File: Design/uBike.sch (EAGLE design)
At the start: 100 parts, among them J10 455-1750-1-ND, J5 C167321, J6 C111196, J9 CONN_08, Q1 B772, Q2 B772, U1 RA-02_LORA, U10 MAX17048, U2 RP2040, U3 W25QXX128MBIT, U4 TMP102, U5 PAM2401, U6 AMS1117-3.3, U8 MCP73831, U9 LSM6DS0, Y1 12MHz

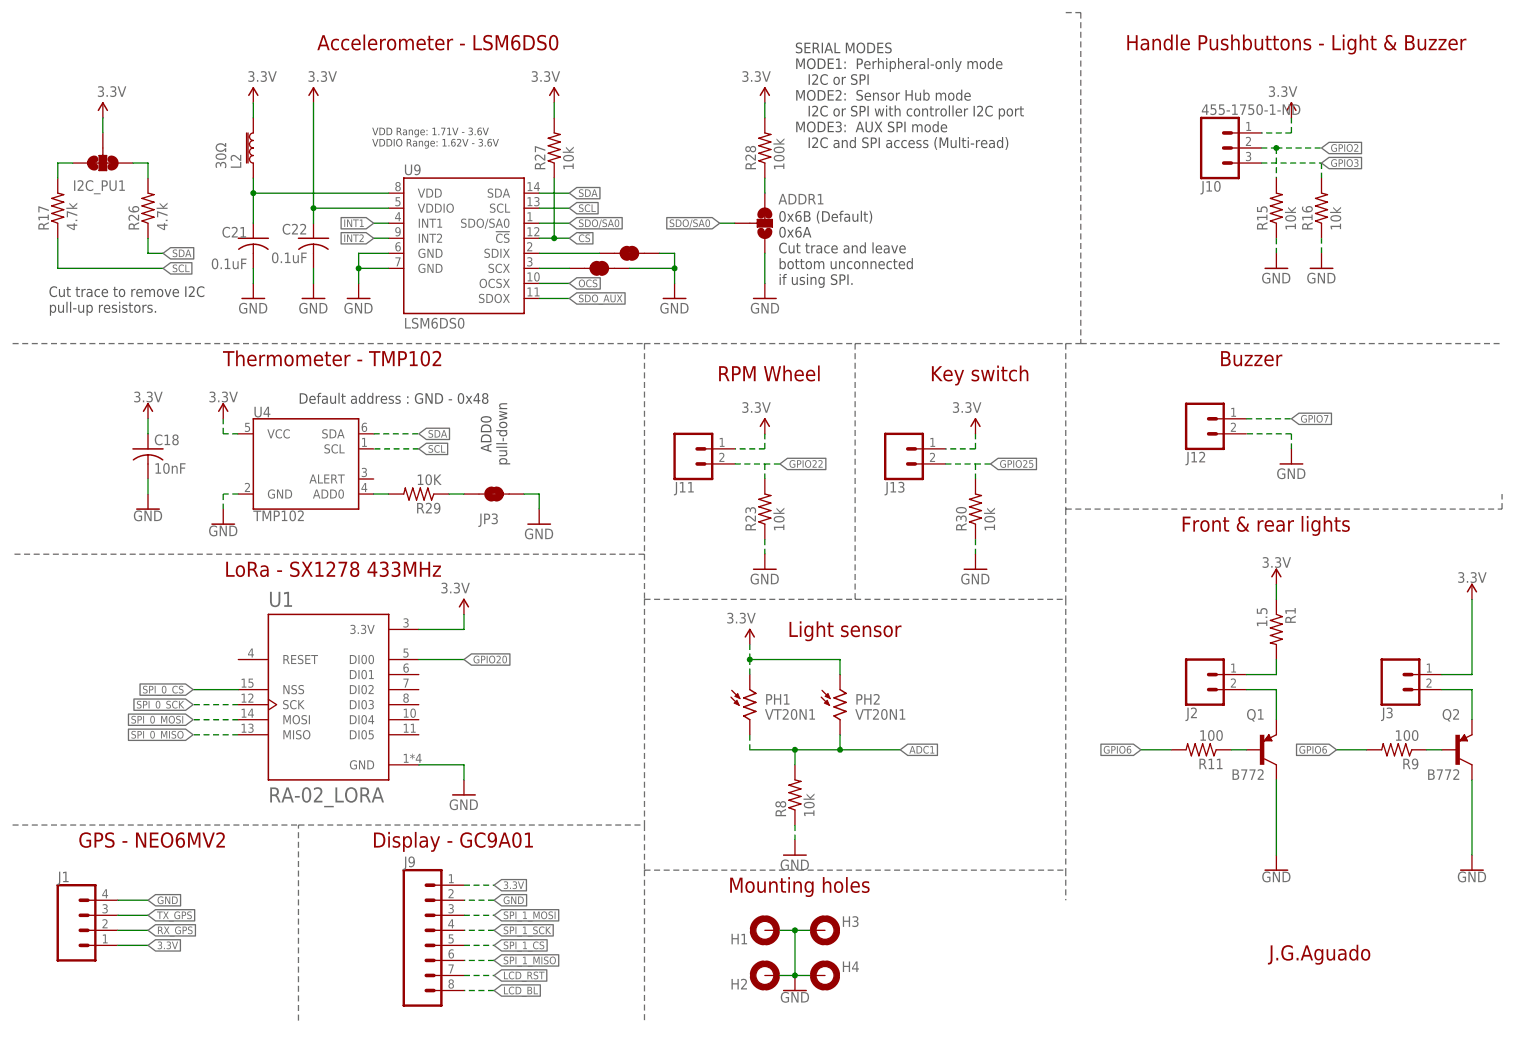
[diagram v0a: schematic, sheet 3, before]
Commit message: New branch replacing Accel & Temp IC with pre-assembled module.
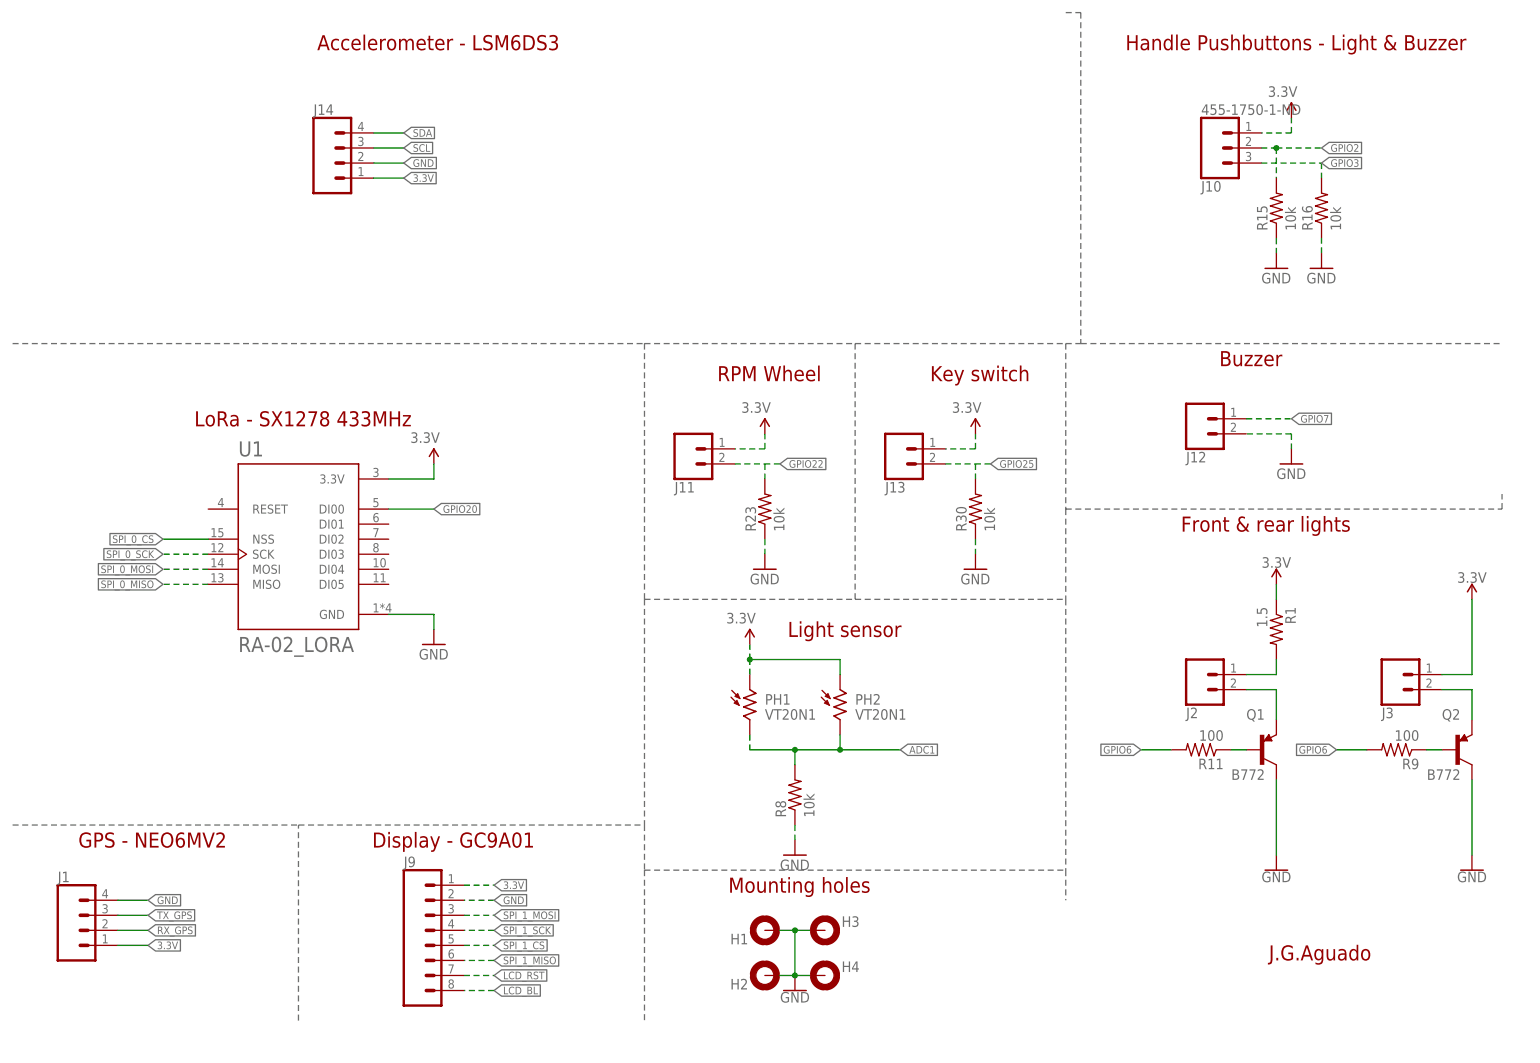
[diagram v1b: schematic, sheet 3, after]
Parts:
- removed ADDR1: JUMPER-SMT_3_1-NC_TRACE_SILK, SparkFun-Jumpers:JUMPER-SMT_3_1-NC_TRACE_SILK
- removed C18: 10nF, rcl:C-USC0402
- removed C21, C22: 0.1uF, rcl:C-USC0402
- removed I2C_PU1: S_MODE, SparkFun-Jumpers:JUMPER-SMT_3_2-NC_TRACE_SILK
- removed JP3: ADD0, SparkFun-Passives:JUMPER-PAD-2-NC_BY_TRACE
- removed L2: 30Ω, SparkFun-Coils:FERRITE_BEAD-0603-30OHM-100MHZ
- removed R17, R26: 4.7k, rcl:R-US_R0402
- removed R27: 10k, rcl:R-US_R0402
- removed R28: 100k, rcl:R-US_R0402
- removed R29: 10K, rcl:R-US_R0402
- removed SDX, SDX1: JUMPER-SMT_2_NC_TRACE_SILK, SparkFun-Jumpers:JUMPER-SMT_2_NC_TRACE_SILK
- removed U4: TMP102, SparkFun-Sensors:TMP102
- removed U9: LSM6DS0, temp:LSM6DS0
- added J14: (no value), SparkFun-Connectors:CONN_04PTH
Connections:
- removed net !CS!: R27.1, U9.!CS!
- removed net ADD0: R29.2, U4.ADD0
- removed net INT1: U9.INT1
- removed net INT2: U9.INT2
- removed net N$15: JP3.1, R29.1
- removed net N$19: I2C_PU1.1, R17.2
- removed net N$20: I2C_PU1.3, R26.2
- removed net N$21: ADDR1.3, R28.1
- removed net OCS: U9.OCSX
- removed net SCX: SDX.2, U9.SCX
- removed net SDI_AUX: SDX1.2, U9.SDIX
- removed net SDO/SA0: ADDR1.2, U9.SDO/SA0
- removed net SDO_AUX: U9.SDOX
- removed net VDD1: C21.1, L2.2, U9.VDD
- net 3.3V: now also J14.1; no longer C18.1, C22.1, I2C_PU1.2, L2.1, R27.2, R28.2, U4.VCC, U9.VDDIO
- net GND: now also J14.2; no longer ADDR1.1, C18.2, C21.2, C22.2, JP3.2, SDX.1, SDX1.1, U4.GND, U9.GND@6, U9.GND@7
- net SCL: now also J14.3; no longer R17.1, U4.SCL, U9.SCL
- net SDA: now also J14.4; no longer R26.1, U4.SDA, U9.SDA
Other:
- note added: "Accelerometer - LSM6DS3"
- note removed: "0x6B (Default) 0x6A Cut trace and leave bottom unconnected if using SPI."
- note removed: "ADD0 pull-down"
- note removed: "Accelerometer - LSM6DS0"
- note removed: "Cut trace to remove I2C pull-up resistors."
- note removed: "Default address : GND - 0x48"
- note removed: "SERIAL MODES MODE1: Perhipheral-only mode I2C or SPI MODE2: Sensor Hub mode I2C or SPI with controller I2C port MODE3: AUX SPI mode I2C and SPI access (Multi-read)"
- note removed: "Thermometer - TMP102"
- note removed: "VDD Range: 1.71V - 3.6V VDDIO Range: 1.62V - 3.6V"
- moved on the sheet: U1

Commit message: Fixed U3 component with W25Q128JVSIQ
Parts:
- C1, C2: LCSC (none) -> C1548
- C10, C17, C20, C3, C4, C5, C6, C7, C8, C9: value 0.1uF -> 100nF
- C12, C16, C19, C29: LCSC (none) -> C12530
- C23, C24: LCSC (none) -> C7171
- D6: LCSC (none) -> C72038
- D7, D8: LCSC (none) -> C64982
- H1, H2, H3, H4: value MOUNT-PAD-ROUND3.0 -> MOUNT-PAD-ROUND; device holes:MOUNT-PAD-ROUND3.0 -> SpaceDIY_connectors:MOUNT-PAD-ROUND
- J5: LCSC (none) -> C167321
- L3, U2: LCSC (none) -> C135262
- Q1, Q2: LCSC (none) -> C24278
- R1: value 1.5 -> 1; LCSC (none) -> C17928
- R25: value 2.0k -> 2k
- S1, S2: LCSC (none) -> C318884
- U3: value W25QXX128MBIT -> W25Q128JVSIQ; device SparkFun-IC-Memory:W25QXX128MBIT-6X5-SKINNY_CENTER -> SamacSys_Parts:W25Q128JVSIQ
- U5: LCSC (none) -> C508238
- Y1: LCSC (none) -> C9002
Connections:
- net 3.3V: now also U3.VCC; no longer U3.VDD
- net QSPI-0: now also U3.DI_(IO0); no longer U3.D0/DI
- net QSPI-1: now also U3.DO_(IO1); no longer U3.D1/DO
- net QSPI-2: now also U3./WP_(IO2); no longer U3.D2/!WP!
- net QSPI-3: now also U3./HOLD_OR_/RESET_(IO3); no longer U3.D3/!HOLD!
- net QSPI-CS: now also U3./CS; no longer U3.!CS!
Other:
- moved on the sheet: C16, C5, J11, J12, J13, J14, J2, J3, PH1, PH2, Q1, Q2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

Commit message: Updated schematic
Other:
- note removed: "J.G.Aguado"
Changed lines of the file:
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@@
 </classes>
 <parts>
-<part name="FRAME1" library="frames" library_urn="urn:adsk.eagle:library:229" deviceset="A4L-LOC" device=""/>
 <part name="H1" library="SpaceDIY_connectors" deviceset="MOUNT-PAD-ROUND" device="" package3d_urn="urn:adsk.eagle:package:14280/1"/>
 <part name="H2" library="SpaceDIY_connectors" deviceset="MOUNT-PAD-ROUND" device="" package3d_urn="urn:adsk.eagle:package:14280/1"/>
@@
 <part name="R11" library="rcl" library_urn="urn:adsk.eagle:library:334" deviceset="R-US_" device="R0402" package3d_urn="urn:adsk.eagle:package:23547/3" value="100"/>
 <part name="GND4" library="SparkFun-PowerSymbols" deviceset="GND" device=""/>
-<part name="FRAME2" library="frames" library_urn="urn:adsk.eagle:library:229" deviceset="A4L-LOC" device=""/>
 <part name="R20" library="rcl" library_urn="urn:adsk.eagle:library:334" deviceset="R-US_" device="R0603" package3d_urn="urn:adsk.eagle:package:23555/3" value="750K"/>
 <part name="R21" library="rcl" library_urn="urn:adsk.eagle:library:334" deviceset="R-US_" device="R0402" package3d_urn="urn:adsk.eagle:package:23547/3" value="100k"/>
@@
 <part name="U1" library="SpaceDIY_modules" deviceset="RA-02_LORA" device=""/>
 <part name="J1" library="SparkFun-Connectors" deviceset="CONN_04" device="PTH"/>
-<part name="FRAME3" library="frames" library_urn="urn:adsk.eagle:library:229" deviceset="A4L-LOC" device=""/>
 <part name="D6" library="SparkFun-LED" deviceset="LED-YELLOW" device="0603" value="Yellow">
 <attribute name="LCSC" value="C72038"/>
@@
 <part name="GND26" library="SparkFun-PowerSymbols" deviceset="GND" device=""/>
 <part name="SUPPLY33" library="SparkFun-PowerSymbols" deviceset="3.3V" device=""/>
+<part name="FRAME1" library="SpaceDIY_symbols" deviceset="A4L-LOC" device=""/>
+<part name="FRAME2" library="SpaceDIY_symbols" deviceset="A4L-LOC" device=""/>
+<part name="FRAME3" library="SpaceDIY_symbols" deviceset="A4L-LOC" device=""/>
 </parts>
 <sheets>
 <sheet>
 <plain>
-<text x="217.17" y="15.24" size="2.54" layer="94">J.G.Aguado</text>
 <wire x1="160.02" y1="175.26" x2="160.02" y2="129.54" width="0.254" layer="95" style="longdash"/>
 <text x="146.304" y="115.316" size="1.27" layer="97" align="center">PIO must be contiguous
@@
 </plain>
 <instances>
-<instance part="FRAME1" gate="G$1" x="0" y="0" smashed="yes">
-<attribute name="DRAWING_NAME" x="217.17" y="20.32" size="2.54" layer="94"/>
-<attribute name="LAST_DATE_TIME" x="217.17" y="10.16" size="2.286" layer="94"/>
-<attribute name="SHEET" x="248.285" y="5.08" size="2.54" layer="94"/>
-</instance>
 <instance part="C1" gate="G$1" x="48.26" y="101.6" smashed="yes" rot="R90">
 <attribute name="NAME" x="41.656" y="101.854" size="1.778" layer="95" font="vector"/>
@@
 <instance part="SUPPLY33" gate="G$1" x="243.84" y="99.06" smashed="yes">
 <attribute name="VALUE" x="243.84" y="101.854" size="1.778" layer="96" align="bottom-center"/>
+</instance>
+<instance part="FRAME1" gate="G$1" x="0" y="0" smashed="yes">
+<attribute name="LAST_DATE_TIME" x="217.17" y="10.16" size="2.286" layer="94"/>
+<attribute name="SHEET" x="227.965" y="5.08" size="2.54" layer="94"/>
+<attribute name="DRAWING_NAME" x="217.17" y="20.32" size="2.54" layer="94"/>
 </instance>
 </instances>
@@
 <wire x1="129.54" y1="81.28" x2="129.54" y2="91.44" width="0.1524" layer="95" style="longdash"/>
 <wire x1="162.56" y1="25.4" x2="162.56" y2="91.44" width="0.1524" layer="95" style="longdash"/>
-<text x="217.17" y="15.24" size="2.54" layer="94">J.G.Aguado</text>
 </plain>
 <instances>
-<instance part="FRAME3" gate="G$1" x="0" y="0" smashed="yes">
-<attribute name="DRAWING_NAME" x="217.17" y="20.32" size="2.54" layer="94"/>
-<attribute name="LAST_DATE_TIME" x="217.17" y="10.16" size="2.286" layer="94"/>
-<attribute name="SHEET" x="248.285" y="5.08" size="2.54" layer="94"/>
-</instance>
 <instance part="R20" gate="G$1" x="76.2" y="50.8" smashed="yes" rot="R90">
 <attribute name="NAME" x="74.7014" y="46.99" size="1.778" layer="95" rot="R90"/>
@@
 <attribute name="NAME" x="203.2" y="58.42" size="1.778" layer="95"/>
 <attribute name="VALUE" x="203.2" y="55.88" size="1.778" layer="96"/>
+</instance>
+<instance part="FRAME2" gate="G$1" x="0" y="0" smashed="yes">
+<attribute name="LAST_DATE_TIME" x="217.17" y="10.16" size="2.286" layer="94"/>
+<attribute name="SHEET" x="227.965" y="5.08" size="2.54" layer="94"/>
+<attribute name="DRAWING_NAME" x="217.17" y="20.32" size="2.54" layer="94"/>
 </instance>
 </instances>
@@
 <text x="201.422" y="109.22" size="2.54" layer="94" font="vector" align="center">Front &amp; rear lights</text>
 <text x="137.922" y="27.94" size="2.54" layer="94" font="vector" align="center">Mounting holes</text>
-<text x="217.17" y="15.24" size="2.54" layer="94">J.G.Aguado</text>
 <text x="145.542" y="170.18" size="2.54" layer="94" font="vector" align="center">Key switch</text>
 <text x="26.162" y="170.18" size="2.54" layer="94" font="vector" align="center">Light sensor</text>
@@
 </plain>
 <instances>
-<instance part="FRAME2" gate="G$1" x="0" y="0" smashed="yes">
-<attribute name="DRAWING_NAME" x="217.17" y="20.32" size="2.54" layer="94"/>
-<attribute name="LAST_DATE_TIME" x="217.17" y="10.16" size="2.286" layer="94"/>
-<attribute name="SHEET" x="248.285" y="5.08" size="2.54" layer="94"/>
-</instance>
 <instance part="H1" gate="G$1" x="132.08" y="20.32" smashed="yes" rot="R180">
 <attribute name="NAME" x="129.286" y="19.7358" size="1.778" layer="95" rot="R180"/>
@@
 <attribute name="NAME" x="119.38" y="94.488" size="1.778" layer="95" font="vector"/>
 </instance>
+<instance part="FRAME3" gate="G$1" x="0" y="0" smashed="yes">
+<attribute name="LAST_DATE_TIME" x="217.17" y="10.16" size="2.286" layer="94"/>
+<attribute name="SHEET" x="227.965" y="5.08" size="2.54" layer="94"/>
+<attribute name="DRAWING_NAME" x="217.17" y="20.32" size="2.54" layer="94"/>
+</instance>
 </instances>

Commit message: Frozen design for August 23 manufacturing batch
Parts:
- removed C20: 100nF, rcl:C-USC0402
- removed C23, C24: 10uF, rcl:CPOL-USA/3216-18R
- removed C25, C26: 4.7uF, rcl:C-USC0402
- removed C29: 2.2uF, SparkFun-Capacitors:2.2UF-0402_TIGHT-10V-10%-X5R
- removed D6: Yellow, SparkFun-LED:LED-YELLOW0603
- removed D7, D8: B340A, SparkFun-DiscreteSemi:DIODE-SCHOTTKY-B340A
- removed H1, H2, H3, H4: MOUNT-PAD-ROUND, SpaceDIY_connectors:MOUNT-PAD-ROUND
- removed J10: 455-1750-1-ND, SparkFun-Connectors:CONN_03
- removed J11, J12, J13, J2, J3, J8: (no value), SparkFun-Connectors:CONN_02
- removed J14: (no value), SparkFun-Connectors:CONN_04PTH
- removed J6: C111196, SparkFun-Connectors:MICRO-SD-PUSH-PUSH-EXT-PIN
- removed J9: CONN_08, SpaceDIY_connectors:CONN_08
- removed L3: 2.2UH3A, SparkFun-Coils:INDUCTOR-IFSC1515AHER2R2M01
- removed Q1, Q2: B772, User-Submitted:TRANSISTOR_PNPSMD-2
- removed R30: 10k, rcl:R-US_R0402
- removed U10: MAX17048, SparkFun-IC-Power:MAX17048DFN8
- removed U2: RP2040, RP2040:RP2040
- removed U3: W25Q128JVSIQ, SamacSys_Parts:W25Q128JVSIQ
- removed U5: PAM2401, SparkFun-IC-Power:PAM2401
- removed U6: AMS1117-3.3, SparkFun-IC-Power:V_REG_LD1117VXXLD1117-SMD
- removed U8: MCP73831, SparkFun-IC-Power:MCP73831
- removed Y1: 12MHz, crystal-geyer_V1_0:KX-7
- added C18: 10uF, rcl:C-USC0603
- added C40: 1uF, rcl:C-USC0603
- added D1, D2: ZMM5V6-M, JLC PCB Basic Parts_loc:ZD_ZMM5V6_ST_MLL34
- added IC1, IC4: TP4056, TP4056:TP4056
- added IC2, IC7: RT9080-33GJ5, SamacSys_Parts:RT9080-33GJ5
- added IC3: MPU-6050, SpaceDIY_IC:MPU-6050
- added IC5: LC709203F/MH, adafruit_sensor:LC709203F/MH
- added IC6: ESP32-S3-MINI-1U-N8, SpaceDIY_modules:ESP32-S3-MINI-1U-N8
- added IC8: TLC555CDR, adafruit:NE555D
- added J18: (no value), SparkFun-Connectors:CONN_04PTH
- added JMP1, JMP2: 0R-JUMPA, jump-0r-smd:0R-JUMPA
- added LED1, LED3: Red, SpaceDIY_semiconductors:LED0603
- added LED2, LED4: Green, SpaceDIY_semiconductors:LED0603
- added PAD1, PAD10, PAD11, PAD12, PAD13, PAD14, PAD15, PAD2, PAD3, PAD4, PAD5, PAD6, PAD7, PAD8, PAD9: (no value), wirepad:SMD2
- added Q5: B772, User-Submitted:TRANSISTOR_PNPSMD-2
- added R17, R28: 1k, SpaceDIY_passive_components:R0402
- added R18: 10K, SpaceDIY_passive_components:R0402
- added R26: 1.2k, SpaceDIY_passive_components:R0402
- added R27: 1K, SpaceDIY_passive_components:R0402
- added R29: 1M, SpaceDIY_passive_components:R0402
- added R36, R37: 5.1k, rcl:R-US_R0603
- added SJ1: (no value), SparkFun:SOLDERJUMPER_2WAYPASTE2&3
- added SJ2, SJ3: SOLDERJUMPERTRACE, SparkFun:SOLDERJUMPERTRACE
- added T1, T6: MMBT2222A, JLC PCB Basic Parts_loc:T_NPN_MMBT2222A-1P_CHANGJ_SOT23-BEC
- added T2: T_P-MOSFET_SI2301CDS-T1-GE3_VISHAY_SOT23-GSD, JLC PCB Basic Parts_loc:T_P-MOSFET_SI2301CDS-T1-GE3_VISHAY_SOT23-GSD
- added T3, T4, T5: T_N-MOSFET_2N7002_CHANGJ_SOT23-GSD, JLC PCB Basic Parts_loc:T_N-MOSFET_2N7002_CHANGJ_SOT23-GSD
- added TP1, TP3: TPTP15R, testpad:TPTP15R
- added U$1: P169H002-CTP, SpaceDIY_connectors:TOUCH-DISPLAY-FPCBOTTOM
- B1: LCSC (none) -> C5377
- C1: value 15pF -> 10uF; device SparkFun-Capacitors:15PF-0402T-50V-5% -> rcl:C-USC0603; LCSC C1548 -> (none)
- C10, C17, C4, C7, C8: value 100nF -> 10uF; device rcl:C-USC0402 -> rcl:C-USC0603
- C11: value 0.1uF -> 100nF; device rcl:C-USC0402 -> rcl:C-USC0603
- C12: value 2.2uF -> 2.2nF; device rcl:C-USC0402 -> rcl:C-USC0603; LCSC C12530 -> (none)
- C13, C15: value 22uF -> 0.1uF
- C14: value 22uF -> 10nF
- C16, C19: value 2.2uF -> 10uF; device rcl:C-USC0402 -> rcl:C-USC0603; LCSC C12530 -> (none)
- C2: value 15pF -> 100u; device SparkFun-Capacitors:15PF-0402T-50V-5% -> SpaceDIY_passive_components:C3528; LCSC C1548 -> C16133
- C3: value 100nF -> 10u; device rcl:C-USC0402 -> rcl:C-USC0603
- C5: value 100nF -> 100n; device rcl:C-USC0402 -> rcl:C-USC0603
- C6: value 100nF -> 0.1uF; device rcl:C-USC0402 -> rcl:C-USC0603
- C9: value 100nF -> 10nF; device rcl:C-USC0402 -> rcl:C-USC0603
- J1: device SparkFun-Connectors:CONN_04PTH -> SpaceDIY_connectors:BAT_CONN-JST-2MM-SMT; LCSC (none) -> C3029440
- J4: device SparkFun-Connectors:CONN_02 -> SpaceDIY_connectors:CONN_06
- J5: value C167321 -> (none); device SparkFun-Connectors:USB_C_4-LAYER-ISOLATED -> SpaceDIY_connectors:CONN_06; LCSC C167321 -> (none)
- J7: value (none) -> USB-C; device SparkFun-Connectors:CONN_02JST-PTH-2 -> SparkFun-Connectors:USB_C_4-LAYER-ISOLATED; LCSC (none) -> C2765186
- PH1, PH2: value VT20N1 -> M9960_11A; device photo-elements:VT20N1 -> photo-elements:M9960_11A
- R1: device rcl:R-US_M1206 -> rcl:R-US_R1206
- R10, R11, R15, R16, R23, R8, R9: device rcl:R-US_R0402 -> SpaceDIY_passive_components:R0402
- R12: value 1k -> 1; device rcl:R-US_R0402 -> rcl:R-US_R1206; LCSC (none) -> C17928
- R13: value 5.1k -> 10K; device rcl:R-US_R0402 -> SpaceDIY_passive_components:R0402
- R14: value 5.1k -> 100; device rcl:R-US_R0402 -> SpaceDIY_passive_components:R0402
- R19: value 1k -> (none); device rcl:R-US_R0402 -> pot:TRIM_US-RJ9W
- R2: value 1k -> 10k; device rcl:R-US_R0402 -> SpaceDIY_passive_components:R0402
- R20: value 750K -> 10K; device rcl:R-US_R0603 -> SpaceDIY_passive_components:R0402
- R21: value 100k -> 10R; device rcl:R-US_R0402 -> SpaceDIY_passive_components:R0402
- R22: value 100k -> 1k; device rcl:R-US_R0402 -> SpaceDIY_passive_components:R0402
- R24: value 750K -> 10k; device rcl:R-US_R0603 -> SpaceDIY_passive_components:R0402
- R25: value 2k -> 1M; device rcl:R-US_R0402 -> SpaceDIY_passive_components:R0402
- R3: value 27 -> 1k; device rcl:R-US_R0603 -> SpaceDIY_passive_components:R0402
- R4: value 27 -> 100; device rcl:R-US_R0603 -> SpaceDIY_passive_components:R0402; LCSC (none) -> C17928
- R5: value 200 -> 10k; device rcl:R-US_R0402 -> SpaceDIY_passive_components:R0402; LCSC (none) -> C17928
- R6: value 1k -> 1.2k; device rcl:R-US_R0402 -> SpaceDIY_passive_components:R0402
- R7: value 10k -> 1K; device rcl:R-US_R0402 -> SpaceDIY_passive_components:R0402
- S1: value MOMENTARY-SWITCH-SPST-SMD-5.2MM-TALL -> Flash; device SparkFun-Switches:MOMENTARY-SWITCH-SPST-SMD-5.2MM-TALL -> SpaceDIY_electromechanical:MOMENTARY-SWITCH-SPST-SMD-5.2MM-TALL; LCSC C318884 -> (none)
- S2: value MOMENTARY-SWITCH-SPST-SMD-5.2MM-TALL -> Reset; device SparkFun-Switches:MOMENTARY-SWITCH-SPST-SMD-5.2MM-TALL -> SpaceDIY_electromechanical:MOMENTARY-SWITCH-SPST-SMD-5.2MM-TALL; LCSC C318884 -> (none)
- U1: value RA-02_LORA -> AMS1117-5VSMD; device SpaceDIY_modules:RA-02_LORA -> SpaceDIY_IC:AMS1117-5VSMD
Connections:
- removed net !RESET!: S2.2, U2.RUN
- removed net 1.1V: C10.1, C11.1, C12.1, U2.LDO_OUT, U2.VDD_1V1
- removed net ADC0: R10.1, R12.1, U2.GPIO26/ADC0
- removed net ADC1: PH1.2, PH2.2, R8.2, U2.GPIO27/ADC1
- removed net ADC2: U2.GPIO28/ADC2
- removed net ADC3: U2.GPIO29/ADC3
- removed net AVDD: C29.1, R5.1, U2.ADC_VDD
- removed net BATT_ALERT: U10.!ALRT, U2.GPIO24
- removed net BOOT: R6.2, S1.2
- removed net DAT1: J6.DAT1, U2.GPIO5
- removed net DAT2: J6.DAT2, U2.GPIO4
- removed net EN_5: R24.1, U5.EN
- removed net GPIO2: J10.2, R15.2, U2.GPIO2
- removed net GPIO20: U1.DI00, U2.GPIO20
- removed net GPIO21: J6.DAT3/!CS!, U2.GPIO21
- removed net GPIO22: J11.2, R23.2, U2.GPIO22
- removed net GPIO23: U2.GPIO23
- removed net GPIO25: J13.2, R30.2, U2.GPIO25
- removed net GPIO3: J10.3, R16.2, U2.GPIO3
- removed net GPIO6: R11.2, R9.2, U2.GPIO6
- removed net GPIO7: J12.1, U2.GPIO7
- removed net LCD_BL: J9.8, U2.GPIO13
- removed net LCD_RST: J9.7, U2.GPIO12
- removed net N$24: R20.1, R21.2, U5.FB
- removed net N$25: L3.2, U5.LX
- removed net N$26: R22.2, U5.RSET
- removed net QSPI-0: U2.QSPI_SD0, U3.DI_(IO0)
- removed net QSPI-1: U2.QSPI_SD1, U3.DO_(IO1)
- removed net QSPI-2: U2.QSPI_SD2, U3./WP_(IO2)
- removed net QSPI-3: U2.QSPI_SD3, U3./HOLD_OR_/RESET_(IO3)
- removed net QSPI-CLK: U2.QSPI_SCLK, U3.CLK
- removed net QSPI-CS: R6.1, R7.1, U2.QSPI_!CS!, U3./CS
- removed net RX_GPS: J1.2, U2.GPIO0
- removed net SPI_0_CS: U1.NSS, U2.GPIO17
- removed net SPI_0_MISO: J6.DAT0/SDO, U1.MISO, U2.GPIO16
- removed net SPI_0_MOSI: J6.CMD/SDI, U1.MOSI, U2.GPIO19
- removed net SPI_0_SCK: J6.CLK/SCK, U1.SCK, U2.GPIO18
- removed net SPI_1_CS: J9.5, U2.GPIO9
- removed net SPI_1_MISO: J9.6, U2.GPIO8
- removed net SPI_1_MOSI: J9.3, U2.GPIO11
- removed net SPI_1_SCK: J9.4, U2.GPIO10
- removed net SWDCK: U2.SWCLK
- removed net SWDIO: U2.SWDIO
- removed net TX_GPS: J1.3, U2.GPIO1
- removed net USB_F_N1: R3.2, U2.USB_D-
- removed net USB_F_P1: R4.2, U2.USB_D+
- removed net USB_N: J5.D-, R3.1
- removed net USB_P: J5.D+, R4.1
- removed net V_BATT: C15.1, C20.1, C23.+, C26.1, J7.1, L3.1, R24.2, U10.CELL, U10.VDD, U5.VIN, U6.IN, U8.VBAT
- removed net V_IN: B1.+, C25.1, R10.2, R19.2, U8.VIN
- new net BAT_VOLT: IC6.IO18, R25.1, R29.2
- new net BUZZER: JMP2-0R.2, R14.2
- new net BUZZ_PB: IC6.IO4, J4.2, J5.2, PAD15.P, R16.2
- new net CC3: J7.CC2, R36.2
- new net CC4: J7.CC1, R37.2
- new net D+: IC6.IO20, J7.D+
- new net D-: IC6.IO19, J7.D-
- new net IO0: IC6.IO0, S1.2
- new net LDR_LH: IC6.IO17, PH1.2, R8.2
- new net LDR_RH: IC6.IO16, PH2.2, R24.2
- new net LEDK: R21.1, U$1.2
- new net LED_FRONT: IC6.IO5, J4.3, J5.3, R11.2
- new net LED_PB: IC6.IO3, J4.1, J5.1, PAD14.P, R15.2
- new net LED_REAR: IC6.IO6, J4.4, J5.4, R9.2
- new net N$15: IC1.!CHRG, R7.2
- new net N$17: PAD12.P, Q5.E
- new net N$18: R3.2, T1.B
- new net N$19: JMP1-0R.2, PAD11.P
- new net N$20: PAD1.P, R12.2
- new net N$33: R21.2, T6.C
- new net N$34: IC8.DIS, R17.2, R19.E
- new net N$35: C11.1, IC8.THR, IC8.TR, R19.A, R19.S
- new net N$36: IC8.Q, JMP2-0R.1
- new net N$37: C9.1, IC8.CV
- new net N$38: IC3.FSYNC, SJ3.2
- new net N$39: IC3.CLKIN, SJ2.2
- new net N$40: C13.1, IC3.REGOUT
- new net N$41: C12.1, IC3.CPOUT
- new net N$43: C14.1, IC3.VLOGIC
- new net N$44: IC3.AD0, SJ1.2
- new net N$46: R22.2, T6.B
- new net N$47: IC4.!STDBY, R28.2
- new net N$48: LED3.C, R27.1
- new net N$49: LED4.C, R28.1
- new net N$50: IC4.PROG, R26.2
- new net N$51: IC4.!CHRG, R27.2
- new net RPM: IC6.IO15, PAD10.P, R23.2
- new net RST: IC6.EN, R13.1, S2.2
- new net RX: IC6.IO2
- new net RXD0: IC6.RXD0, J18.4
- new net SENS: IC6.IO21, R3.1
- new net TFT_BL: IC6.IO45, R22.1
- new net TFT_CS: IC6.IO7, U$1.8
- new net TFT_DC: IC6.IO39, U$1.7
- new net TFT_MISO: IC6.IO37
- new net TFT_MOSI: IC6.IO35, U$1.10
- new net TFT_RST: IC6.IO40, U$1.11
- new net TFT_SCK: IC6.IO36, U$1.9
- new net TP_INT: IC6.IO33, U$1.16
- new net TP_RST: IC6.IO34, U$1.15
- new net TX: IC6.IO1
- new net TXD0: IC6.TXD0, J18.3
- new net UC_BUZZER: IC6.IO8, J4.5, J5.5, JMP2-0R.3
- new net VBAT: C16.1, C18.1, C40.1, IC4.BAT, IC5.VDD, IC7.EN, IC7.VIN, J1.+, R25.2
- new net VBAT_1: C1.1, C8.1, IC1.BAT, IC2.EN, IC2.VIN, PAD5.P
- new net VBUS: C17.1, IC4.CE, IC4.VCC, J7.VBUS, LED3.A, LED4.A
- new net VSENS: C15.1, IC3.VDD, PAD9.P, PH1.1, PH2.1, R18.1, R20.1, SJ1.1, T2.D, U$1.17, U$1.3
- new net V_BUZZ: IC8.R, IC8.V+, R17.1
- new net V_DYN_UR: B1.+, C2.+, C3.1, D2.C, R4.1, TP1.TP, U1.IN
- new net V_REG: C4.1, C5.1, IC1.CE, IC1.VCC, LED1.A, LED2.A, TP3.TP, U1.OUT
- net 3.3V: now also C10.1, IC2.VOUT, IC6.3V3, IC7.VOUT, J18.1, JMP1-0R.3, PAD13.P, R12.1, R13.2, R2.1, T2.S; no longer C16.1, C17.1, C24.+, C3.1, C4.1, C5.1, C8.1, C9.1, J1.1, J10.1, J11.1, J13.1, J14.1, J3.1, J6.VCC, J9.1, PH1.1, PH2.1, R5.2, R7.2, U1.3.3V, U2.LDO_IN, U2.USB_VDD, U2.VDDIO, U3.VCC, U6.OUT
- net 5V: now also JMP1-0R.1; no longer C13.1, C14.1, D7.C, D8.C, J4.1, R20.2, U5.OUT
- net GND: now also C1.2, C18.2, C2.-, C40.2, D1.A, IC1.GND, IC1.TEMP, IC2.GND, IC3.GND, IC4.GND, IC4.TEMP, IC5.TEST, IC5.VSS, IC6.GND_1, IC6.GND_10, IC6.GND_11, IC6.GND_12, IC6.GND_13, IC6.GND_14, IC6.GND_15, IC6.GND_16, IC6.GND_17, IC6.GND_18, IC6.GND_19, IC6.GND_2, IC6.GND_20, IC6.GND_21, IC6.GND_22, IC6.GND_23, IC6.GND_24, IC6.GND_25, IC6.GND_26, IC6.GND_27, IC6.GND_28, IC6.GND_29, IC6.GND_3, IC6.GND_30, IC6.GND_31, IC6.GND_32, IC6.GND_4, IC6.GND_5, IC6.GND_6, IC6.GND_7, IC6.GND_8, IC6.GND_9, IC7.GND, IC8.GND, J1.-, J18.2, J4.6, J5.6, J7.GND, PAD6.P, Q5.C, R24.1, R26.1, R29.1, R36.1, R37.1, R5.2, R6.1, SJ1.3, SJ2.1, SJ3.1, T1.E, T3.S, T4.S, T5.S, T6.E, U$1.1, U$1.12, U$1.18, U$1.5, U$1.6; no longer C1.1, C2.1, C20.2, C23.-, C24.-, C25.2, C26.2, C29.2, D7.A, D8.A, H1.MOUNT, H2.MOUNT, H3.MOUNT, H4.MOUNT, J1.4, J12.2, J14.2, J4.2, J5.GND, J6.DET, J6.GND, J7.2, J9.2, Q1.C, Q2.C, R12.2, R13.2, R14.2, R21.1, R22.1, R25.1, R30.1, U10.CTG, U10.GND, U10.QSTRT, U2.GND, U2.TESTEN, U3.GND, U5.AGND, U5.PGND, U6.GND, U8.VSS
- net N$1: now also PAD3.P; no longer J2.1
- net N$10: now also PAD8.P; no longer J8.2
- net N$11: now also LED1.C, R7.1; no longer D6.A, R19.1
- net N$12: now also LED2.C, R10.1; no longer J5.CC2, R14.1
- net N$13: now also IC1.PROG, R6.2; no longer D6.C, U8.STAT
- net N$14: now also PAD7.P; no longer J8.1
- net N$16: now also Q5.B, R14.1; no longer R25.2, U8.PROG
- net N$2: now also T4.G; no longer Q2.B
- net N$3: now also IC1.!STDBY, R10.2; no longer R2.2, U2.XOUT
- net N$4: now also PAD4.P, T3.D; no longer J2.2, Q1.E
- net N$5: now also T3.G; no longer Q1.B
- net N$6: now also PAD2.P, T4.D; no longer J3.2, Q2.E
- net N$7: now also D2.A, R5.1, T5.G; no longer C2.2, U2.XIN, Y1.2
- net N$8: now also D1.C, R4.2, T5.D; no longer C1.2, R2.1, Y1.1
- net N$9: now also R2.2, T1.C, T2.G; no longer J5.CC1, R13.1
- net SCL: now also IC3.SCL, IC5.SCL, IC6.IO41, R18.2, U$1.13; no longer J14.3, U10.SCL, U2.GPIO15
- net SDA: now also IC3.SDA, IC5.SDA, IC6.IO42, R20.2, U$1.14; no longer J14.4, U10.SDA, U2.GPIO14
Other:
- note added: "Battery charger"
- note added: "Battery monitoring"
- note added: "Generator voltage regulation"
- note added: "Handle pushbuttons"
- note added: "Headers"
- note added: "High switch for power supply"
- note added: "IMU"
- note added: "Microcontroller"
- note added: "R4 [k] - IBAT [mA] ------------------------ 10 - 130 5 - 250 4 - 300 3 - 400 2 - 580 1.66 - 690 1.5 - 780 1.33 - 900 1.2 - 1000"
- note added: "Reset & Flash switches"
- note added: "Serial port"
- note added: "Touch display"
- note added: "USB-C"
- note added: "Vbat to 3.3V"
- note removed: "16MB / 128mbit Flash"
- note removed: "3.3V voltage regulator"
- note removed: "5V voltage regulator"
- note removed: "600mA out VIN: 2.5V-6V"
- note removed: "Accelerometer - LSM6DS3"
- note removed: "Battery management unit"
- note removed: "Boot"
- note removed: "Charge current: I_CHG = 1000 / R_PROG R_PROG=2k : I_CHG=500mA"
- note removed: "Display - GC9A01"
- note removed: "GPS - NEO6MV2"
- note removed: "Handle Pushbuttons - Light & Buzzer"
- note removed: "I2C_ADDR: 0x36"
- note removed: "Key switch"
- note removed: "Lithium-Polymer battery charger (1-cell)"
- note removed: "LoRa - SX1278 433MHz"
- note removed: "Microcontroller - RP2040"
- note removed: "Mounting holes"
- note removed: "PIO must be contiguous for SDIO DAT pins but can fall back to SPI1"
- note removed: "Reset"
- note removed: "USB Connector"
- note removed: "V_BATT should be a single- cell LiPo battery."
- note removed: "uSD Connector"
